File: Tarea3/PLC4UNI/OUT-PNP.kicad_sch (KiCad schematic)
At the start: 8 parts, among them U5 AT3H4B-CUH-S

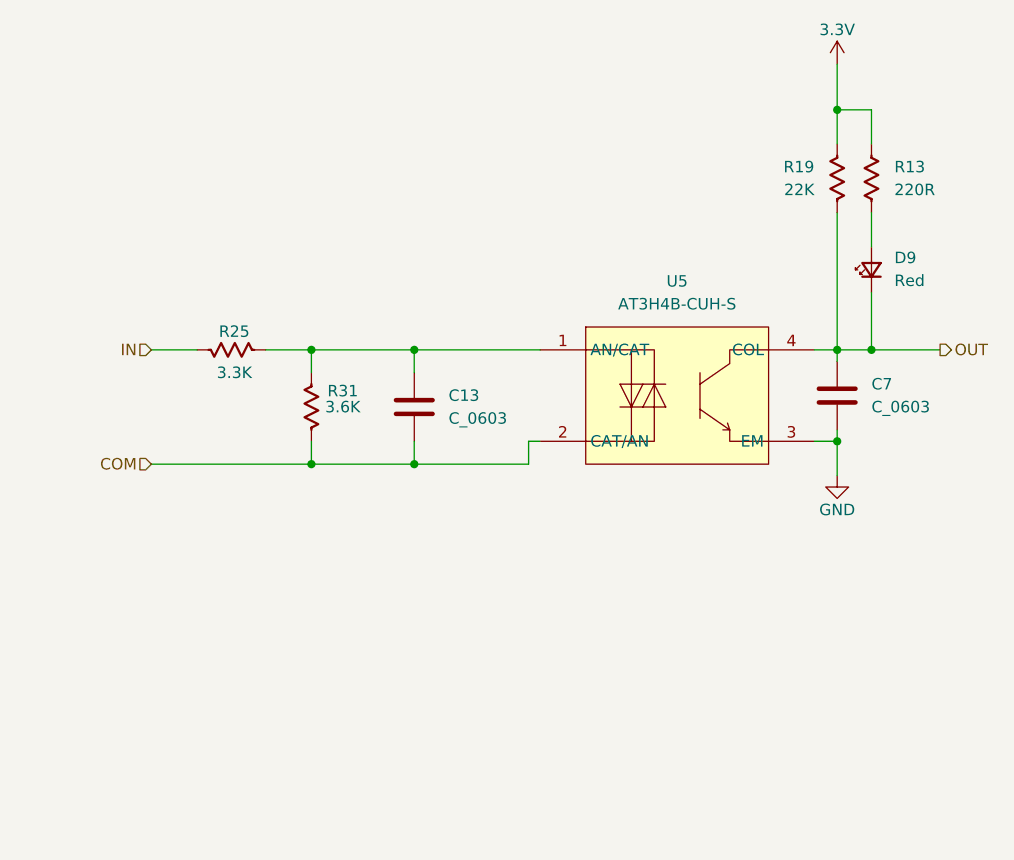
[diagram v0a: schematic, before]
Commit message: Cambio de directorio [Tarea2->CAD]
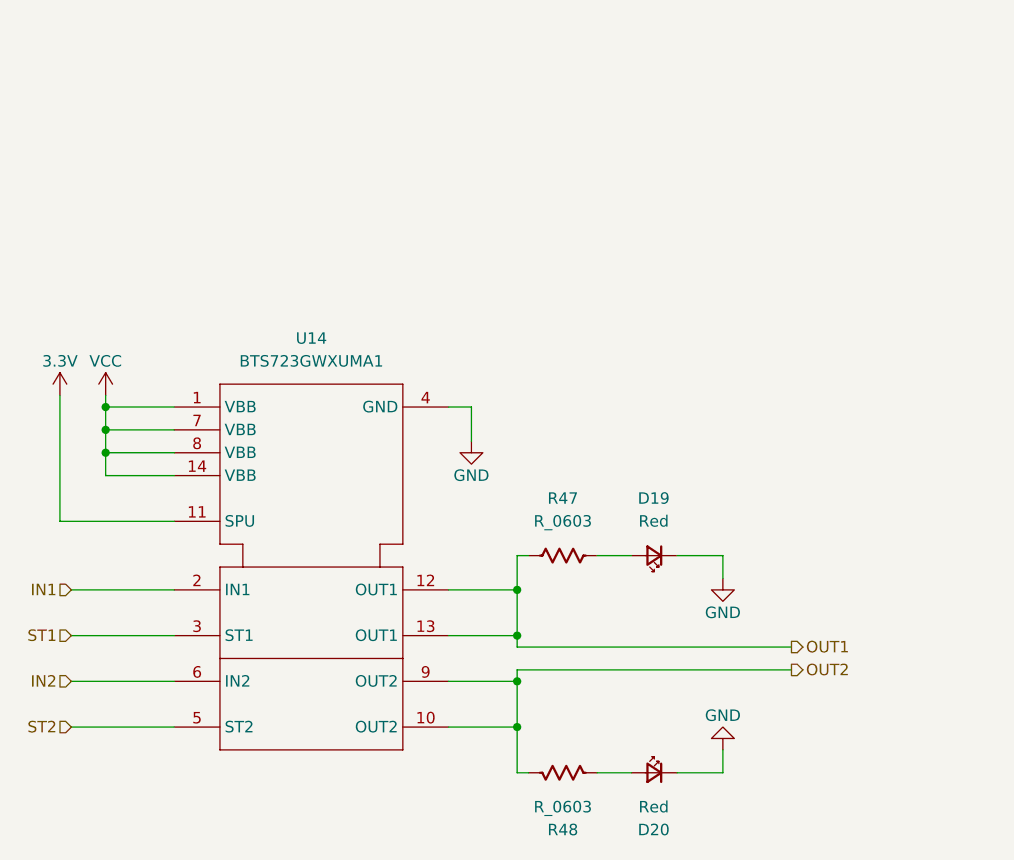
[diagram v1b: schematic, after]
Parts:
- removed C13, C7: C_0603, PCM_Capacitor_SMD_AKL:C_0603_1608Metric, symbol PCM_Capacitor_US_AKL:C_0603
- removed D9: Red, PCM_SparkFun-LED:LED_0603_1608Metric_Red, symbol PCM_SparkFun-LED:LED_Red_0603
- removed R13: 220R, PCM_Resistor_SMD_AKL:R_0603_1608Metric, symbol PCM_Resistor_US_AKL:R_0603
- removed R19: 22K, PCM_Resistor_SMD_AKL:R_0603_1608Metric, symbol PCM_Resistor_US_AKL:R_0603
- removed R25: 3.3K, PCM_Resistor_SMD_AKL:R_0603_1608Metric, symbol PCM_Resistor_US_AKL:R_0603
- removed R31: 3.6K, PCM_Resistor_SMD_AKL:R_0603_1608Metric, symbol PCM_Resistor_US_AKL:R_0603
- removed U5: AT3H4B-CUH-S, EasyEDA:SSOP-4_L2.7-W4.6-P1.27-LS7.0-TL, symbol EasyEDA:AT3H4B-CUH-S
- added D19, D20: Red, PCM_SparkFun-LED:LED_0603_1608Metric_Red, symbol PCM_SparkFun-LED:LED_Red_0603
- added R47, R48: R_0603, PCM_Resistor_SMD_AKL:R_0603_1608Metric, symbol PCM_Resistor_US_AKL:R_0603
- added U14: BTS723GWXUMA1, EasyEDA:SOIC-14_L8.7-W3.9-P1.27-LS6.0-BL, symbol EasyEDA:BTS723GWXUMA1
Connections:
- net 3.3V: now also U14.11 (SPU)
- net GND: now also D19.1 (K), D20.1 (K), U14.4 (GND)
- new net: D20.2 (A), R48.2
- new net: D19.2 (A), R47.2
- new net IN1: U14.2 (IN1)
- new net IN2: U14.6 (IN2)
- new net OUT1: R47.1, U14.12 (OUT1), U14.13 (OUT1)
- new net OUT2: R48.1, U14.10 (OUT2), U14.9 (OUT2)
- new net ST1: U14.3 (ST1)
- new net ST2: U14.5 (ST2)
- new net VCC: U14.1 (VBB), U14.14 (VBB), U14.7 (VBB), U14.8 (VBB)
